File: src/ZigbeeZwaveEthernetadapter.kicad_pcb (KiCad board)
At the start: 2 copper layers, 100 x 100 mm, 1 part

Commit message: Mod: Schematic and PCB-Layout, finished new Version.
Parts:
- removed G0: LOGO, drawings:elektronik-emblem_3x3.5_solder
- added C101: 100µF, Capacitor_SMD:C_0805_2012Metric_Pad1.18x1.45mm_HandSolder, F.Cu at (152.5, 82.0)
- added C102: 10µF, Capacitor_SMD:C_0805_2012Metric_Pad1.18x1.45mm_HandSolder, F.Cu at (152.5, 87.0)
- added D101: GN, LED_SMD:LED_0805_2012Metric_Pad1.15x1.40mm_HandSolder, F.Cu at (174.0, 106.0)
- added D102: YE, LED_SMD:LED_0805_2012Metric_Pad1.15x1.40mm_HandSolder, F.Cu at (176.5, 106.0)
- added G***: LOGO, Drawings_User:elektronik-emblem_10x11.6_solder, B.Cu at (175.5, 90.0)
- added H101: MountingHole, MountingHole:MountingHole_2.7mm_M2.5_DIN965, F.Cu at (123.5, 73.5)
- added H102: MountingHole, MountingHole:MountingHole_2.7mm_M2.5_DIN965, F.Cu at (161.5, 73.5)
- added H103: MountingHole, MountingHole:MountingHole_2.7mm_M2.5_DIN965, F.Cu at (161.5, 96.5)
- added H104: MountingHole, MountingHole:MountingHole_2.7mm_M2.5_DIN965, F.Cu at (123.5, 96.5)
- added H105: MountingHole, MountingHole:MountingHole_3.2mm_M3_DIN965, F.Cu at (136.5, 73.5)
- added H106: MountingHole, MountingHole:MountingHole_3.2mm_M3_DIN965, F.Cu at (183.5, 73.5)
- added H107: MountingHole, MountingHole:MountingHole_3.2mm_M3_DIN965, F.Cu at (183.5, 106.5)
- added H108: MountingHole, MountingHole:MountingHole_3.2mm_M3_DIN965, F.Cu at (136.5, 106.5)
- added J101: Conn_02x06_Odd_Even, Connector_PinSocket_2.54mm:PinSocket_2x06_P2.54mm_Vertical, F.Cu at (162.5, 78.7)
- added J102: Conn_01x06, Connector_PinSocket_2.54mm:PinSocket_1x06_P2.54mm_Vertical, F.Cu at (139.1, 98.0)
- added J104: Conn_01x06, Connector_PinSocket_2.54mm:PinSocket_1x06_P2.54mm_Vertical, F.Cu at (144.0, 72.0)
- added J105: Conn_02x05_Odd_Even, Connector_PinHeader_2.54mm:PinHeader_2x05_P2.54mm_Vertical, F.Cu at (168.4, 74.5)
- added J106: USB4125-GF-A, Connector_User:GCT_USB4125-GF-A, F.Cu at (160.0, 107.8)
- added J107: USB_B_Micro, Connector_USB:USB_Micro-B_Amphenol_10118194_Horizontal, F.Cu at (145.0, 107.2)
- added J108: Barrel_Jack, Connector_User:CUI_PJ-037A, F.Cu at (131.0, 105.0)
- added JP101: SolderJumper_2_Open, Jumper:SolderJumper-2_P1.3mm_Open_TrianglePad1.0x1.5mm, F.Cu at (172.5, 79.0)
- added JP102: SolderJumper_2_Open, Jumper:SolderJumper-2_P1.3mm_Open_TrianglePad1.0x1.5mm, F.Cu at (175.0, 79.0)
- added JP103: SolderJumper_2_Open, Jumper:SolderJumper-2_P1.3mm_Open_TrianglePad1.0x1.5mm, F.Cu at (177.5, 79.0)
- added R101: 5.1k, Resistor_SMD:R_0805_2012Metric_Pad1.20x1.40mm_HandSolder, F.Cu at (169.5, 106.0)
- added R102: 5.1k, Resistor_SMD:R_0805_2012Metric_Pad1.20x1.40mm_HandSolder, F.Cu at (167.0, 106.0)
- added R103: 100R, Resistor_SMD:R_0805_2012Metric_Pad1.20x1.40mm_HandSolder, F.Cu at (168.0, 88.5)
- added R104: 100R, Resistor_SMD:R_0805_2012Metric_Pad1.20x1.40mm_HandSolder, F.Cu at (170.5, 87.5)
- added U101: TLV1117-33, Package_TO_SOT_SMD:SOT-223-3_TabPin2, F.Cu at (147.4, 84.5)
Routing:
- net +5V: track 0.00 -> 93.1 mm, vias 0 -> 1
- net +3V3: track 0.00 -> 66.4 mm, vias 0 -> 2
- net GND: track 0.00 -> 57.1 mm, vias 0 -> 25
- net /RXD: track 0.00 -> 39.0 mm
- net /GPIO_D: track 0.00 -> 38.6 mm
- net /GPIO_C: track 0.00 -> 33.2 mm
- net /TXD: track 0.00 -> 31.7 mm
- net /GPIO_B: track 0.00 -> 26.8 mm
- net Net-(D102-A): track 0.00 -> 19.0 mm
- net Net-(D101-A): track 0.00 -> 18.0 mm
- net Net-(J106-CC1): track 0.00 -> 11.9 mm
- net Net-(J106-CC2): track 0.00 -> 8.10 mm
- net /GPIO_2: track 0.00 -> 4.37 mm
- net /GPIO_3: track 0.00 -> 4.36 mm
- net /GPIO_4: track 0.00 -> 4.34 mm
- added copper zone on B.Cu, net GND
- added copper zone on F.Cu, net GND
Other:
- board size 100 x 100 mm -> 67 x 40 mm
- board text added: "Only one plug can be used at a time!"
- board text added: "RX"
- board text added: "RaZberry 7 Pro"
- board text added: "TX"
- board text added: "WIZ750SR"

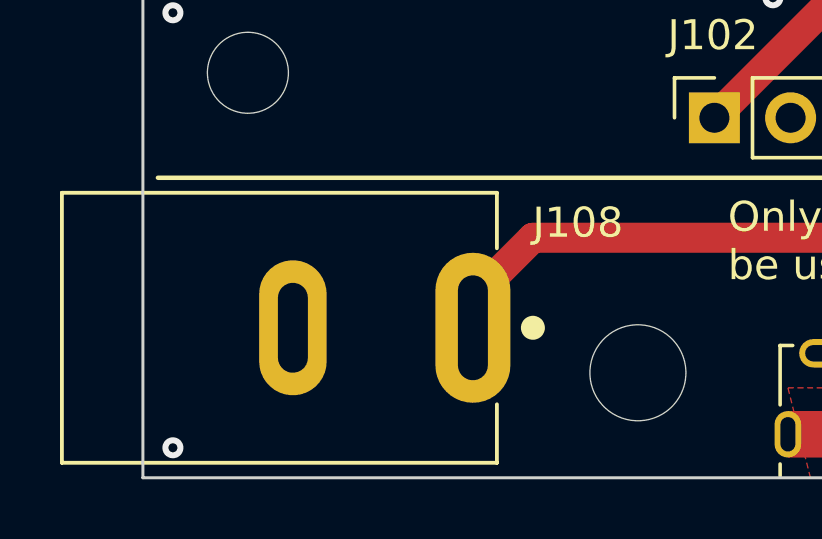
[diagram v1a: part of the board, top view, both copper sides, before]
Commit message: Mod: ZigbeeZwaveEthernetadapter.kicad_pcb, removed DRC errors and warnings.
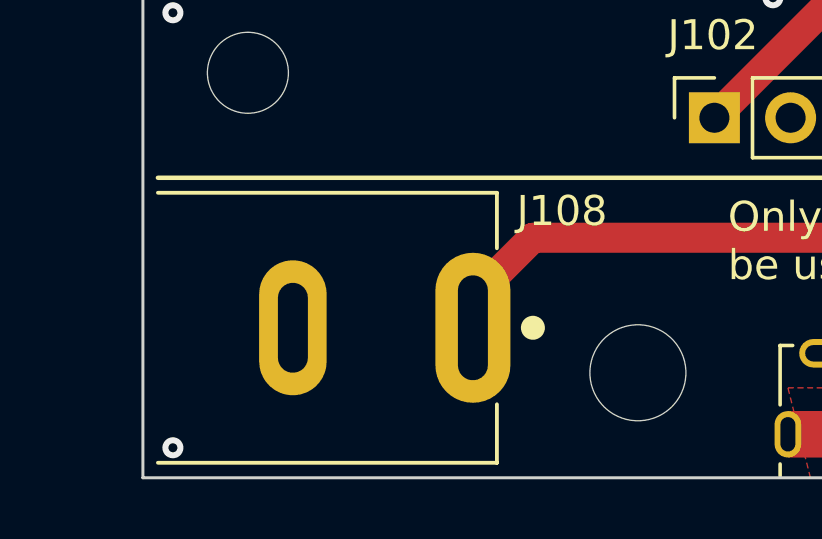
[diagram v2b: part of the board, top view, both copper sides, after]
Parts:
- J108: footprint Connector_User:CUI_PJ-037A -> Connector_User:CUI_PJ-037A_Board-Edge
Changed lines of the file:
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@@
   (title_block
     (title "Raspberry Pi UART to Ethernet Adapter")
-    (date "2024-01-26")
+    (date "2024-01-27")
     (rev "A")
     (company "ElektroNik Zoller")
@@
     (pad "" np_thru_hole circle (at 0 0) (size 2.7 2.7) (drill 2.7) (layers "*.Cu" "*.Mask"))
   )
-  (footprint "Connector_User:CUI_PJ-037A" (layer "F.Cu")
+  (footprint "Connector_User:CUI_PJ-037A_Board-Edge" (layer "F.Cu")
     (at 131 105 180)
     (property "Manufacturer Part No." "PJ-037A")
@@
     (property "ki_keywords" "DC power barrel jack connector")
     (attr through_hole)
-    (fp_text reference "J108" (at -3.5 3.5) (layer "F.SilkS")
+    (fp_text reference "J108" (at -2.97 3.89 180) (layer "F.SilkS")
         (effects (font (size 1.000913 1.000913) (thickness 0.15)))
     )
-    (fp_text value "Barrel_Jack" (at 6.302586 5.781935) (layer "F.Fab") hide
+    (fp_text value "Barrel_Jack" (at 6.302586 5.781935 180) (layer "F.Fab") hide
         (effects (font (size 1.001205 1.001205) (thickness 0.15)))
     )
-    (fp_text user "${REFERENCE}" (at 1.5 3.5 180) (layer "F.Fab")
-        (effects (font (size 1 1) (thickness 0.15)))
-    )
-    (fp_line (start -0.8 -4.5) (end 13.7 -4.5)
+    (fp_text user "Board edge ->" (at 11 -3) (layer "Cmts.User")
+        (effects (font (size 1 1) (thickness 0.15)) (justify right))
+    )
+    (fp_text user "${REFERENCE}" (at 1.094 3.636 180) (layer "F.Fab")
+        (effects (font (size 1 1) (thickness 0.15)))
+    )
+    (fp_line (start -0.8 -4.5) (end 10.5 -4.5)
       (stroke (width 0.127) (type solid)) (layer "F.SilkS"))
     (fp_line (start -0.8 -2.55) (end -0.8 -4.5)
@@
     (fp_line (start -0.8 4.5) (end -0.8 2.65)
       (stroke (width 0.127) (type solid)) (layer "F.SilkS"))
-    (fp_line (start 13.7 -4.5) (end 13.7 4.5)
-      (stroke (width 0.127) (type solid)) (layer "F.SilkS"))
-    (fp_line (start 13.7 4.5) (end -0.8 4.5)
+    (fp_line (start 10.5 4.5) (end -0.8 4.5)
       (stroke (width 0.127) (type solid)) (layer "F.SilkS"))
     (fp_circle (center -2 0) (end -1.8 0)
       (stroke (width 0.4) (type solid)) (fill none) (layer "F.SilkS"))
+    (fp_line (start 11 4.6) (end 11 -4.6)
+      (stroke (width 0.12) (type default)) (layer "Cmts.User"))
     (fp_line (start -1.55 -2.25) (end -1.55 2.35)
       (stroke (width 0.05) (type solid)) (layer "F.CrtYd"))

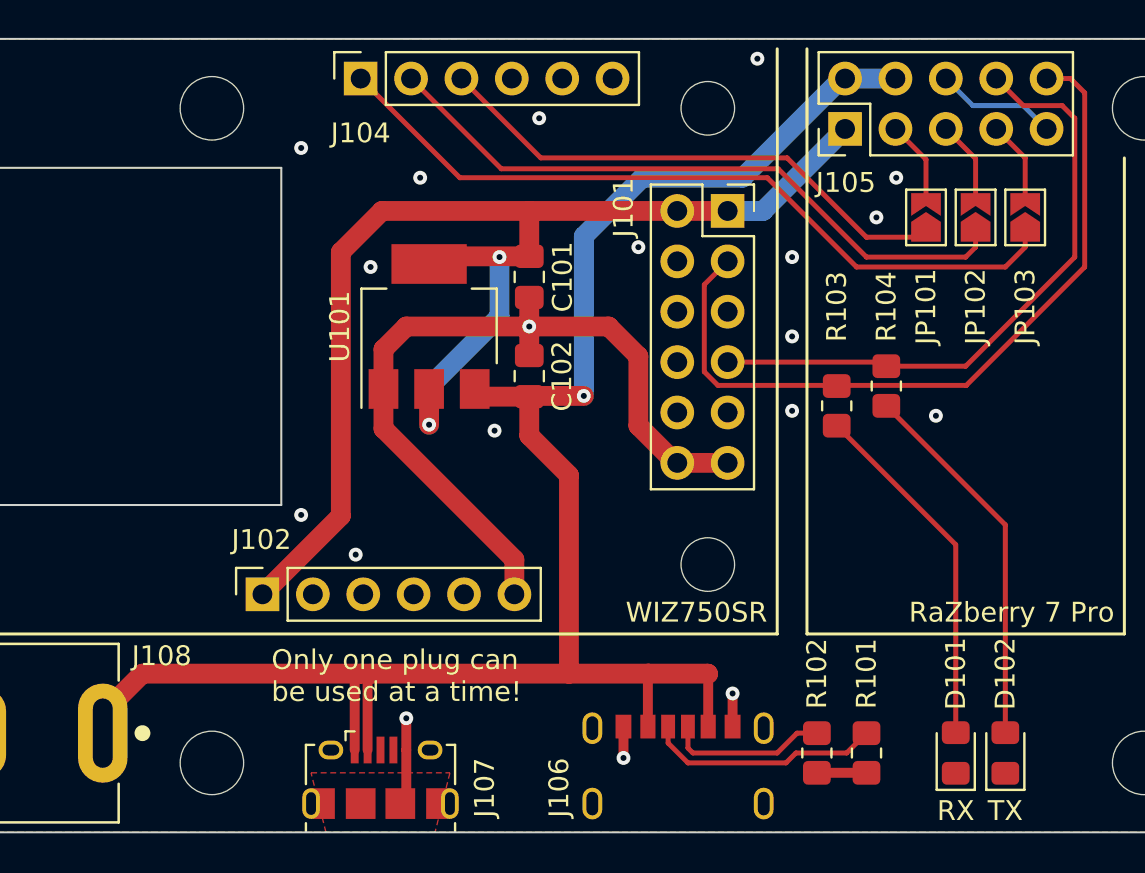
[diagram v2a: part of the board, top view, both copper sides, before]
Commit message: Mod: LEDs for RXD and TXD, changed from Pull-Down to Pull-Up resistors and changed their value. Re-exported all the files.
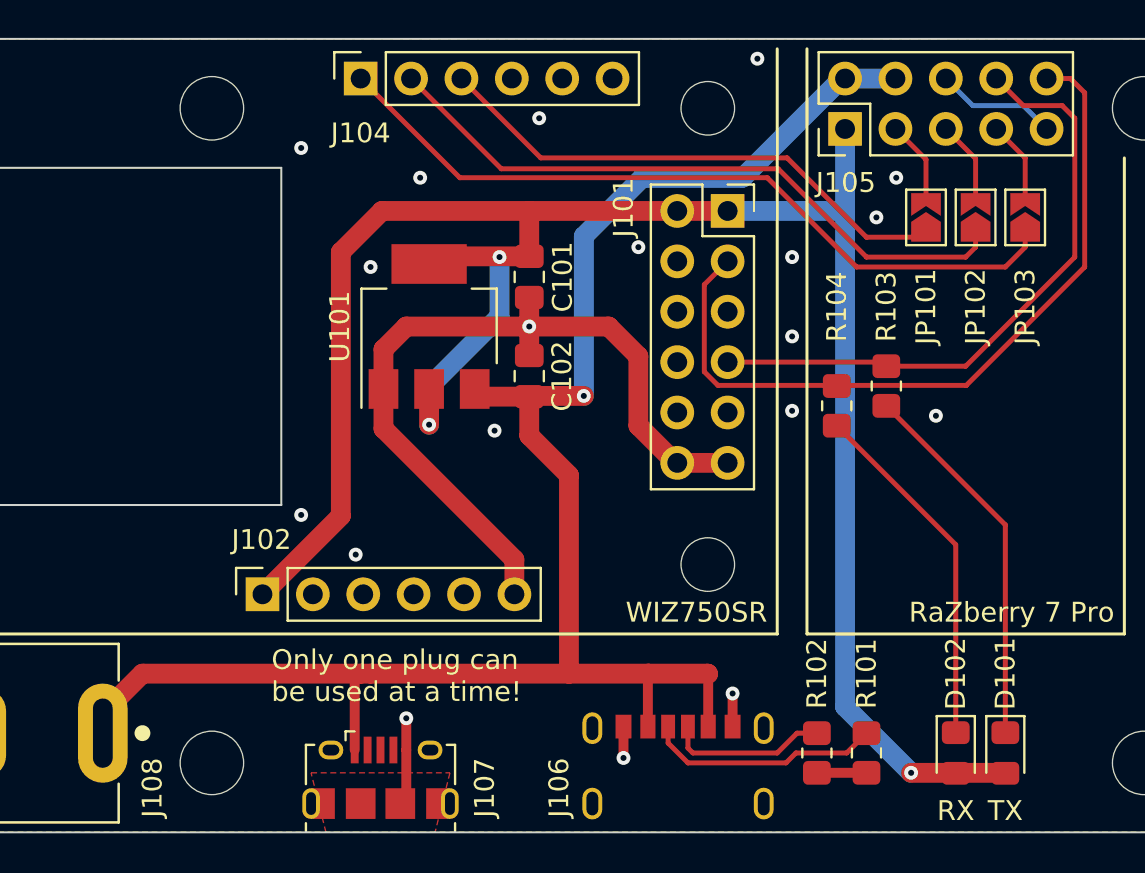
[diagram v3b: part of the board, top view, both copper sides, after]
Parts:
- D102: value YE -> GN
- R103, R104: value 100R -> 470R
- moved R103 2.69 mm to (170.5, 87.5), turned to 90 degrees
- moved R104 2.69 mm to (168.0, 88.5), turned to 90 degrees
- moved D101 2.50 mm to (176.5, 106.0), turned to -90 degrees
- moved D102 2.50 mm to (174.0, 106.0), turned to -90 degrees
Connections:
- D101 pad 1: GND -> Net-(D101-K)
- D101 pad 2: Net-(D101-A) -> +3V3
- D102 pad 1: GND -> Net-(D102-K)
- D102 pad 2: Net-(D102-A) -> +3V3
- J107 pad 2: +5V -> unconnected-(J107-D--Pad2)
- R103 pad 1: /RXD -> Net-(D101-K)
- R103 pad 2: Net-(D101-A) -> /TXD
- R104 pad 1: /TXD -> Net-(D102-K)
- R104 pad 2: Net-(D102-A) -> /RXD
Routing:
- net +3V3: track 66.4 -> 103.3 mm, vias 2 -> 3
- net Net-(D102-A): track 19.0 -> 0.00 mm
- net Net-(D101-K): track 0.00 -> 19.0 mm
- net Net-(D102-K): track 0.00 -> 18.0 mm
- net Net-(D101-A): track 18.0 -> 0.00 mm
- net +5V: track 93.1 -> 89.4 mm
